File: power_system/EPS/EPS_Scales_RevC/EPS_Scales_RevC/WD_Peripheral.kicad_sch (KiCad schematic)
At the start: 40 parts, among them J15 Conn_01x04, J16 Conn_01x04, U10 TLV1704

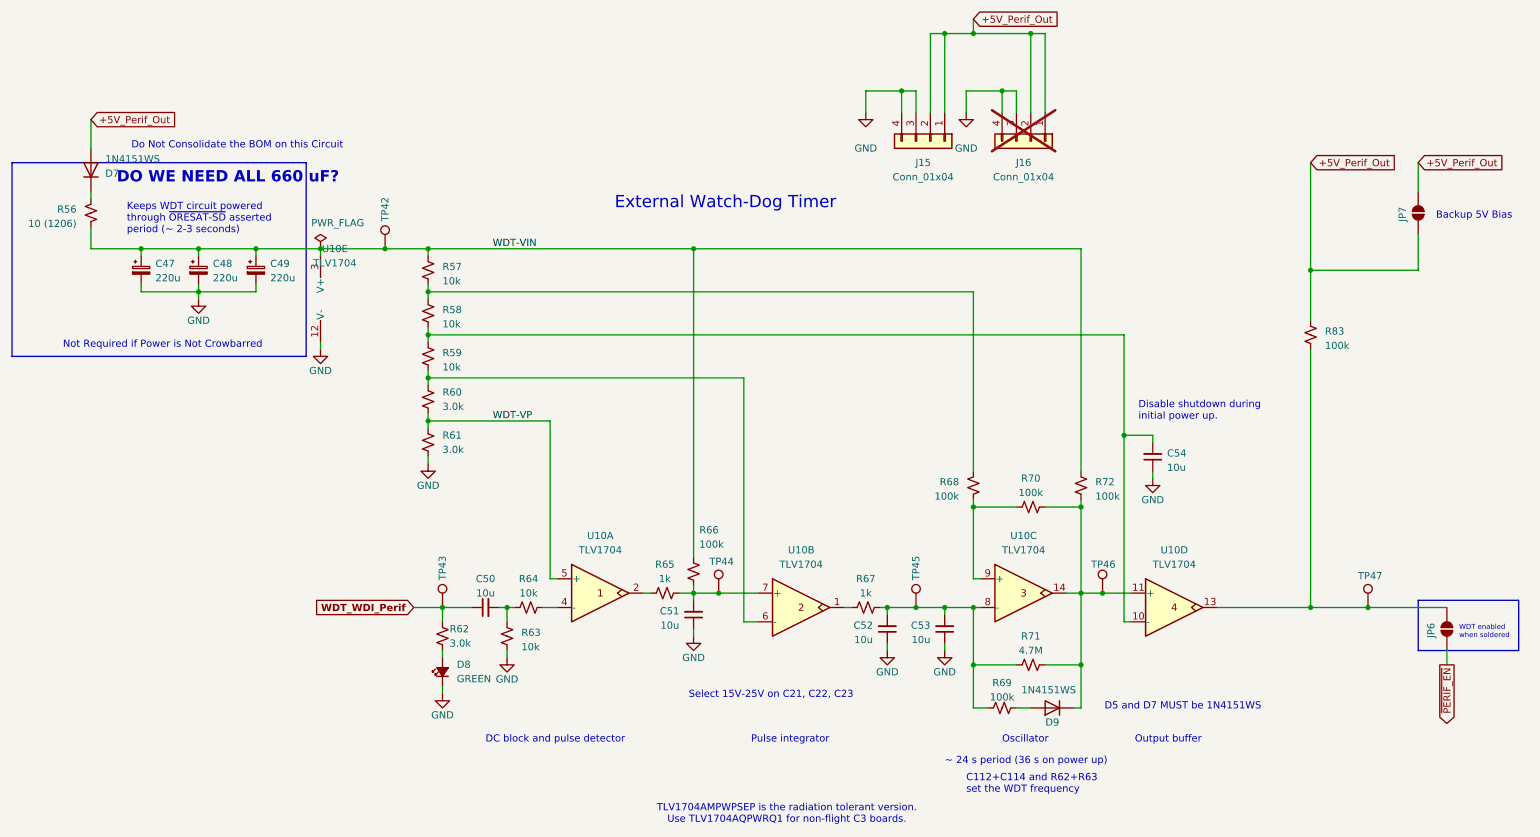
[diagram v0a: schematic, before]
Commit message: Rev C Schematic DONE
Components were finalized in meeting with Andrew Greenberg today, footprints have been assigned and specific component sizes and values have also been confirmed. Moving to layout for the first dev board of the SCALES EPS board.
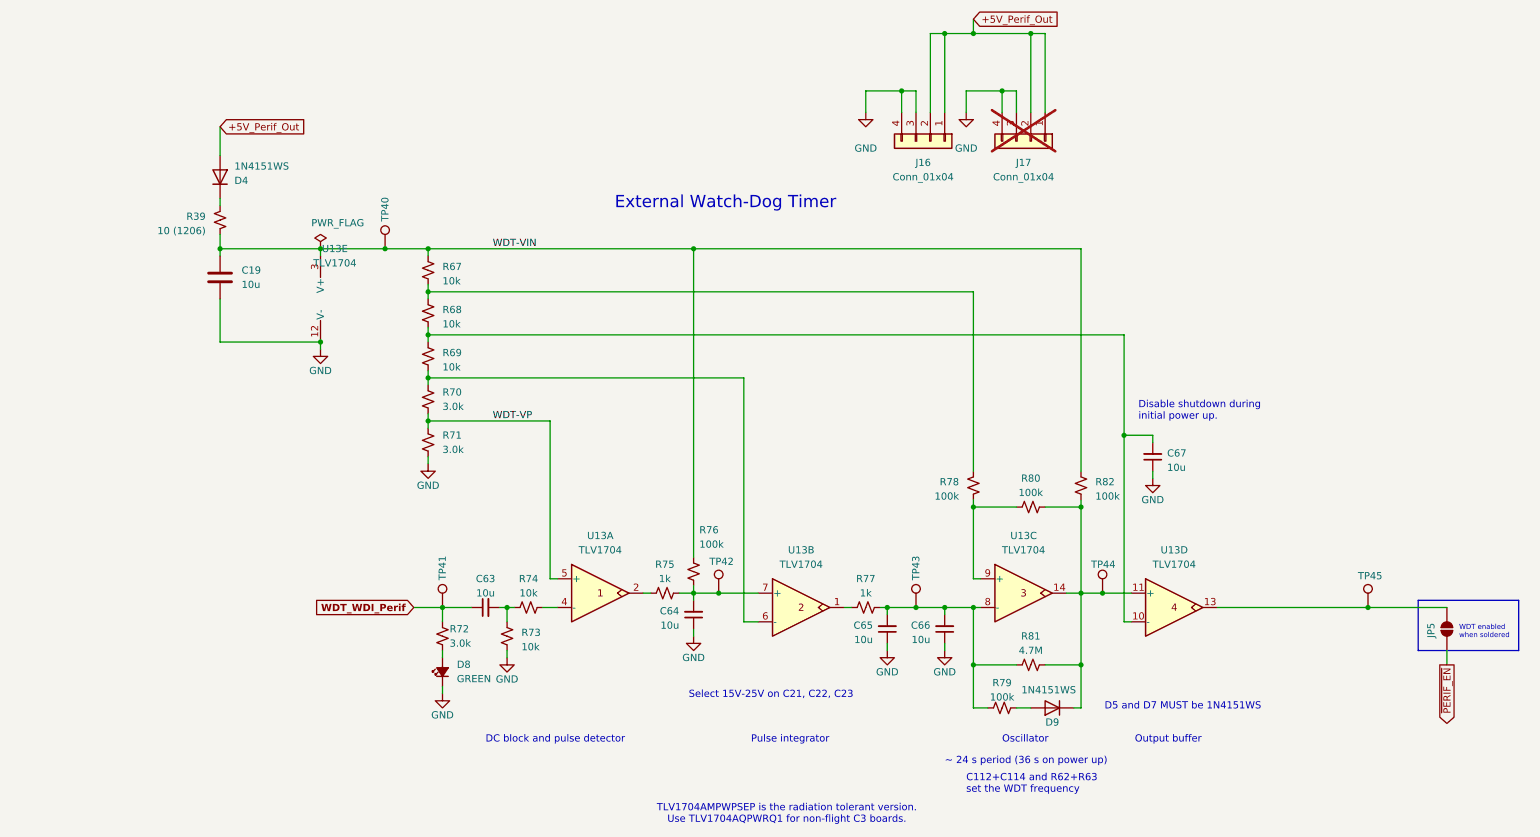
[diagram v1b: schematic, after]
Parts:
- removed C47, C48, C49: 220u, Capacitor_Tantalum_SMD:CP_EIA-7361-38_AVX-V, symbol Device:C_Polarized_Small
- removed D7: 1N4151WS, Diode_SMD:D_SOD-323, symbol Device:D
- removed JP7: SolderJumper_2_Open, Jumper:SolderJumper-2_P1.3mm_Open_RoundedPad1.0x1.5mm, symbol Jumper:SolderJumper_2_Open
- removed R56: 10 (1206), Resistor_SMD:R_1206_3216Metric, symbol Device:R_Small_US
- removed R83: 100k, Resistor_SMD:R_0603_1608Metric, symbol Device:R_Small_US
- added C19: 10u, Resistor_SMD:R_1210_3225Metric, symbol Device:C
- added D4: 1N4151WS, Diode_SMD:D_SOD-323, symbol Device:D
- added R39: 10 (1206), Resistor_SMD:R_1206_3216Metric, symbol Device:R_Small_US
- C63: renamed from C50; footprint Capacitor_SMD:C_1210_3225Metric -> Resistor_SMD:R_1210_3225Metric
- C64: renamed from C51; footprint Capacitor_SMD:C_1210_3225Metric -> Resistor_SMD:R_1210_3225Metric
- C65: renamed from C52; footprint Capacitor_SMD:C_1210_3225Metric -> Resistor_SMD:R_1210_3225Metric
- C66: renamed from C53; footprint Capacitor_SMD:C_1210_3225Metric -> Resistor_SMD:R_1210_3225Metric
- C67: renamed from C54; footprint Capacitor_SMD:C_1210_3225Metric -> Resistor_SMD:R_1210_3225Metric
- renumbered J15 to J16, J16 to J17, JP6 to JP5, R57 to R67, R58 to R68, R59 to R69, R60 to R70, R61 to R71, R62 to R72, R63 to R73, R64 to R74, R65 to R75, R66 to R76, R67 to R77, R68 to R78, R69 to R79, R70 to R80, R71 to R81, R72 to R82, TP42 to TP40, TP43 to TP41, TP44 to TP42, TP45 to TP43, TP46 to TP44, TP47 to TP45, U10 to U13
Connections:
- net +5V_Perif_Out: now also D4.2 (A)
- net GND: now also C19.2
- net WDT-VIN: now also C19.1, R39.2
- new net: D4.1 (K), R39.1
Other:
- note removed: "Backup 5V Bias"
- note removed: "DO WE NEED ALL 660 uF?"
- note removed: "Do Not Consolidate the BOM on this Circuit"
- note removed: "Keeps WDT circuit powered through ~{ORESAT-SD} asserted period (~ 2-3 seconds)"
- note removed: "Not Required if Power is Not Crowbarred"

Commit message: Rev C Layout #2 electric boogaloo
Yes
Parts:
- C19, C63, C64, C65, C66, C67: footprint Resistor_SMD:R_1210_3225Metric -> Capacitor_SMD:C_1210_3225Metric
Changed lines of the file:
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@@
 			)
 		)
-		(property "Footprint" "Resistor_SMD:R_1210_3225Metric"
+		(property "Footprint" "Capacitor_SMD:C_1210_3225Metric"
 			(at 217.17 96.52 0)
 			(effects
@@
 			)
 		)
-		(property "Footprint" "Resistor_SMD:R_1210_3225Metric"
+		(property "Footprint" "Capacitor_SMD:C_1210_3225Metric"
 			(at 170.18 127 0)
 			(effects
@@
 			)
 		)
-		(property "Footprint" "Resistor_SMD:R_1210_3225Metric"
+		(property "Footprint" "Capacitor_SMD:C_1210_3225Metric"
 			(at 180.34 127 0)
 			(effects
@@
 			)
 		)
-		(property "Footprint" "Resistor_SMD:R_1210_3225Metric"
+		(property "Footprint" "Capacitor_SMD:C_1210_3225Metric"
 			(at 135.89 124.46 0)
 			(effects
@@
 			)
 		)
-		(property "Footprint" "Resistor_SMD:R_1210_3225Metric"
+		(property "Footprint" "Capacitor_SMD:C_1210_3225Metric"
 			(at 53.0352 68.58 0)
 			(effects
@@
 			)
 		)
-		(property "Footprint" "Resistor_SMD:R_1210_3225Metric"
+		(property "Footprint" "Capacitor_SMD:C_1210_3225Metric"
 			(at 99.06 123.19 0)
 			(effects

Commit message: Some oopsies but fixed Them, routed one segment
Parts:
- R67: renamed from R39; LCSC (none) -> C17903
- R68: renamed from R67; LCSC (none) -> C13564
- R69: renamed from R68; LCSC (none) -> C13564
- R70: renamed from R69; LCSC (none) -> C13564
- R71: renamed from R70; LCSC (none) -> C4211
- R72: renamed from R71; LCSC (none) -> C4211
- R73: renamed from R72; LCSC (none) -> C4211
- R74: renamed from R73; LCSC (none) -> C13564
- R75: renamed from R74; LCSC (none) -> C13564
- R76: renamed from R75; LCSC (none) -> C13163
- R77: renamed from R76; LCSC (none) -> C14675
- R78: renamed from R77; LCSC (none) -> C13163
- R79: renamed from R78; LCSC (none) -> C14675
- R80: renamed from R79; LCSC (none) -> C14675
- R81: renamed from R80; LCSC (none) -> C14675
- R83: renamed from R82; LCSC (none) -> C14675
- U13: LCSC (none) -> C181596
- renumbered C19 to C56, C63 to C57, C64 to C58, C65 to C59, C66 to C60, C67 to C61, D4 to D7, JP5 to JP4, R81 to R82, TP40 to TP39, TP41 to TP40, TP42 to TP41, TP43 to TP42, TP44 to TP43, TP45 to TP44

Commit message: Schematic and Layout changes
Made all watch dogs powered by +5v perif supply
All INAs are now powered by the 3.3v OBC supply.
DFU 16 connectors were updated to through hole versions.
Redundant test points were removed.
Layout needs work to reroute new items.
Still need to add I2C buffer
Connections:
- net +5V_Perif_Out renamed +5V_Perif
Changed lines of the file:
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@@
+		)
+	)
+	(text_box "This watchdog is left floating due to being pulled low at the input side of the load switch."
+		(exclude_from_sim no)
+		(at 238.125 100.965 0)
+		(size 31.115 12.7)
+		(margins 0.9525 0.9525 0.9525 0.9525)
+		(stroke
+			(width 0)
+			(type solid)
+		)
+		(fill
+			(type none)
+		)
+		(effects
+			(font
+				(size 1.27 1.27)
+			)
+			(justify left top)
 		)
 	)
@@
 			)
 			(justify left bottom)
-		)
-	)
-	(global_label "+5V_Perif_Out"
-		(shape input)
-		(at 185.42 19.05 0)
-		(fields_autoplaced yes)
-		(effects
-			(font
-				(size 1.27 1.27)
-			)
-			(justify left)
-		)
-		(property "Intersheetrefs" "${INTERSHEET_REFS}"
-			(at 201.8914 19.05 0)
-			(effects
-				(font
-					(size 1.27 1.27)
-				)
-				(justify left)
-				(hide yes)
-			)
 		)
 	)
@@
 		)
 	)
-	(global_label "+5V_Perif_Out"
+	(global_label "+5V_Perif"
+		(shape input)
+		(at 185.42 19.05 0)
+		(fields_autoplaced yes)
+		(effects
+			(font
+				(size 1.27 1.27)
+			)
+			(justify left)
+		)
+		(property "Intersheetrefs" "${INTERSHEET_REFS}"
+			(at 197.7186 19.05 0)
+			(effects
+				(font
+					(size 1.27 1.27)
+				)
+				(justify left)
+				(hide yes)
+			)
+		)
+	)
+	(global_label "+5V_Perif"
 		(shape input)
 		(at 52.07 38.1 0)
@@
 		)
 		(property "Intersheetrefs" "${INTERSHEET_REFS}"
-			(at 68.5414 38.1 0)
+			(at 64.3686 38.1 0)
 			(effects
 				(font

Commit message: Schematic Revisions
Added updated block diagram
Added Individual watch dog setups for each subsystem. Resistor and Capacitor values must be modified to reflect desired time range.
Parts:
- removed J17: Conn_01x04, Connector_PinSocket_2.54mm:PinSocket_1x04_P2.54mm_Vertical, symbol Connector_Generic:Conn_01x04
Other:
- moved on the sheet: J16

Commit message: Layout Complete
Added I2C buffer
Found replacement inductor for 10uH
Added footprints for new components
Last thing missing is changing the solder mask sizing on most footprints to remove the errors.
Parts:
- D7, D9: footprint Diode_SMD:D_SOD-323 -> RevC Footprints:SODFL2512X100N
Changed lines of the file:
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@@
 			)
 		)
-		(property "Footprint" "Diode_SMD:D_SOD-323"
+		(property "Footprint" "RevC Footprints:SODFL2512X100N"
 			(at 199.39 140.97 0)
 			(effects
@@
 			)
 		)
-		(property "Footprint" "Diode_SMD:D_SOD-323"
+		(property "Footprint" "RevC Footprints:SODFL2512X100N"
 			(at 52.07 46.99 0)
 			(effects

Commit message: Revert "Luca branch v2"
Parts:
- added J17: Conn_01x04, Connector_PinSocket_2.54mm:PinSocket_1x04_P2.54mm_Vertical, symbol Connector_Generic:Conn_01x04
- D7, D9: footprint RevC Footprints:SODFL2512X100N -> Diode_SMD:D_SOD-323
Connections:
- net +5V_Perif: now also J17.1 (Pin_1), J17.2 (Pin_2)
- net GND: now also J17.3 (Pin_3), J17.4 (Pin_4)
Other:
- moved on the sheet: J16
